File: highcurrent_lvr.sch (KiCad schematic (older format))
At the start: 8 parts, among them J1 Conn_01x02_Female, J2 Conn_01x02_Female

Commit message: fixed pcb layout
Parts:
- removed D1, D2, D3: LED, LED_SMD:LED_0805_2012Metric_Pad1.15x1.40mm_HandSolder, symbol Device:LED
- removed R7, R8, R9: 1k, Resistor_SMD:R_0805_2012Metric_Pad1.20x1.40mm_HandSolder, symbol Device:R
- renumbered J1 to POWER_IN1, J2 to POWER_OUT1
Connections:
- net GND: now also POWER_OUT1.1 (Pin_1); no longer POWER_OUT1.2 (Pin_2)
- net vout: now also POWER_OUT1.2 (Pin_2); no longer POWER_OUT1.1 (Pin_1)
- no-connect marks 0 -> 2
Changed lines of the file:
@@
 	1    0    0    -1
 $EndComp
-$Comp
-L Device:R R8
-U 1 1 602D43E7
-P 5000 5500
-F 0 "R8" H 5070 5546 50  0000 L CNN
-F 1 "1k" H 5070 5455 50  0000 L CNN
-F 2 "Resistor_SMD:R_0805_2012Metric_Pad1.20x1.40mm_HandSolder" V 4930 5500 50  0001 C CNN
-F 3 "~" H 5000 5500 50  0001 C CNN
-	1    5000 5500
-	0    -1   -1   0
-$EndComp
-$Comp
-L Device:R R9
-U 1 1 602D53F2
-P 5000 5300
-F 0 "R9" H 5070 5346 50  0000 L CNN
-F 1 "1k" H 5070 5255 50  0000 L CNN
-F 2 "Resistor_SMD:R_0805_2012Metric_Pad1.20x1.40mm_HandSolder" V 4930 5300 50  0001 C CNN
-F 3 "~" H 5000 5300 50  0001 C CNN
-	1    5000 5300
-	0    -1   -1   0
-$EndComp
-Wire Wire Line
-	4400 5300 4850 5300
-Wire Wire Line
-	4400 5700 4850 5700
-Wire Wire Line
-	4400 5500 4850 5500
 Wire Wire Line
 	800  800  800  1000
@@
 Wire Wire Line
 	1200 1000 1200 800
-Text Label 4400 5700 0    50   ~ 0
-error
-Text Label 4400 5300 0    50   ~ 0
-supp_error
-Text Label 4400 5500 0    50   ~ 0
-vout
-$Comp
-L Device:R R7
-U 1 1 604ED0D2
-P 5000 5700
-F 0 "R7" H 5070 5746 50  0000 L CNN
-F 1 "1k" H 5070 5655 50  0000 L CNN
-F 2 "Resistor_SMD:R_0805_2012Metric_Pad1.20x1.40mm_HandSolder" V 4930 5700 50  0001 C CNN
-F 3 "~" H 5000 5700 50  0001 C CNN
-	1    5000 5700
-	0    -1   -1   0
-$EndComp
 $Sheet
 S 6150 3050 950  500
@@
 F0 "Cutoff" 50
 F1 "Cutoff.sch" 50
-F2 "Vin" I L 6150 3150 50
+F2 "vin" I L 6150 3150 50
 F3 "Vout" O R 7100 3150 50
 F4 "GND" O R 7100 3250 50
@@
 Text Label 5650 3150 0    50   ~ 0
 reg_out
-$Comp
-L Device:LED D1
-U 1 1 602FA7E4
-P 5500 5300
-F 0 "D1" H 5493 5045 50  0000 C CNN
-F 1 "LED" H 5493 5136 50  0000 C CNN
-F 2 "LED_SMD:LED_0805_2012Metric_Pad1.15x1.40mm_HandSolder" H 5500 5300 50  0001 C CNN
-F 3 "~" H 5500 5300 50  0001 C CNN
-	1    5500 5300
-	-1   0    0    1
-$EndComp
-Wire Wire Line
-	5150 5300 5350 5300
-$Comp
-L Device:LED D2
-U 1 1 602FC079
-P 5500 5500
-F 0 "D2" H 5493 5245 50  0000 C CNN
-F 1 "LED" H 5493 5336 50  0000 C CNN
-F 2 "LED_SMD:LED_0805_2012Metric_Pad1.15x1.40mm_HandSolder" H 5500 5500 50  0001 C CNN
-F 3 "~" H 5500 5500 50  0001 C CNN
-	1    5500 5500
-	-1   0    0    1
-$EndComp
-Wire Wire Line
-	5150 5500 5350 5500
-$Comp
-L power:GND #PWR0115
-U 1 1 602FC629
-P 6200 6800
-F 0 "#PWR0115" H 6200 6550 50  0001 C CNN
-F 1 "GND" H 6205 6627 50  0000 C CNN
-F 2 "" H 6200 6800 50  0001 C CNN
-F 3 "" H 6200 6800 50  0001 C CNN
-	1    6200 6800
-	1    0    0    -1
-$EndComp
-$Comp
-L Device:LED D3
-U 1 1 602FC62F
-P 5500 5700
-F 0 "D3" H 5493 5445 50  0000 C CNN
-F 1 "LED" H 5493 5536 50  0000 C CNN
-F 2 "LED_SMD:LED_0805_2012Metric_Pad1.15x1.40mm_HandSolder" H 5500 5700 50  0001 C CNN
-F 3 "~" H 5500 5700 50  0001 C CNN
-	1    5500 5700
-	-1   0    0    1
-$EndComp
-Wire Wire Line
-	5150 5700 5350 5700
 Wire Wire Line
 	3750 3150 4200 3150
@@
 add reverse polarity protection
 $Comp
-L Connector:Conn_01x02_Female J1
+L Connector:Conn_01x02_Female POWER_IN1
 U 1 1 602E4815
 P 3550 3250
-F 0 "J1" H 3578 3226 50  0000 L CNN
+F 0 "POWER_IN1" H 3578 3226 50  0000 L CNN
 F 1 "Conn_01x02_Female" H 3578 3135 50  0000 L CNN
 F 2 "TerminalBlock_Phoenix:TerminalBlock_Phoenix_MKDS-1,5-2_1x02_P5.00mm_Horizontal" H 3550 3250 50  0001 C CNN
@@
 $EndComp
 $Comp
-L Connector:Conn_01x02_Female J2
+L Connector:Conn_01x02_Female POWER_OUT1
 U 1 1 602E8D12
-P 7850 3150
-F 0 "J2" H 7878 3126 50  0000 L CNN
-F 1 "Conn_01x02_Female" H 7878 3035 50  0000 L CNN
-F 2 "TerminalBlock_Phoenix:TerminalBlock_Phoenix_MKDS-1,5-2_1x02_P5.00mm_Horizontal" H 7850 3150 50  0001 C CNN
-F 3 "~" H 7850 3150 50  0001 C CNN
-	1    7850 3150
-	1    0    0    -1
+P 7850 3250
+F 0 "POWER_OUT1" H 7878 3226 50  0000 L CNN
+F 1 "Conn_01x02_Female" H 7878 3135 50  0000 L CNN
+F 2 "TerminalBlock_Phoenix:TerminalBlock_Phoenix_MKDS-1,5-2_1x02_P5.00mm_Horizontal" H 7850 3250 50  0001 C CNN
+F 3 "~" H 7850 3250 50  0001 C CNN
+	1    7850 3250
+	1    0    0    1
 $EndComp
-Wire Wire Line
-	5650 5300 6200 5300
-Wire Wire Line
-	5650 5500 6200 5500
-Connection ~ 6200 5500
-Wire Wire Line
-	6200 5500 6200 5300
-Wire Wire Line
-	5650 5700 6200 5700
-Connection ~ 6200 5700
-Wire Wire Line
-	6200 5700 6200 5500
-Wire Wire Line
-	6200 5700 6200 6800
+NoConn ~ 7250 3900
+NoConn ~ 5450 3900
 $EndSCHEMATC

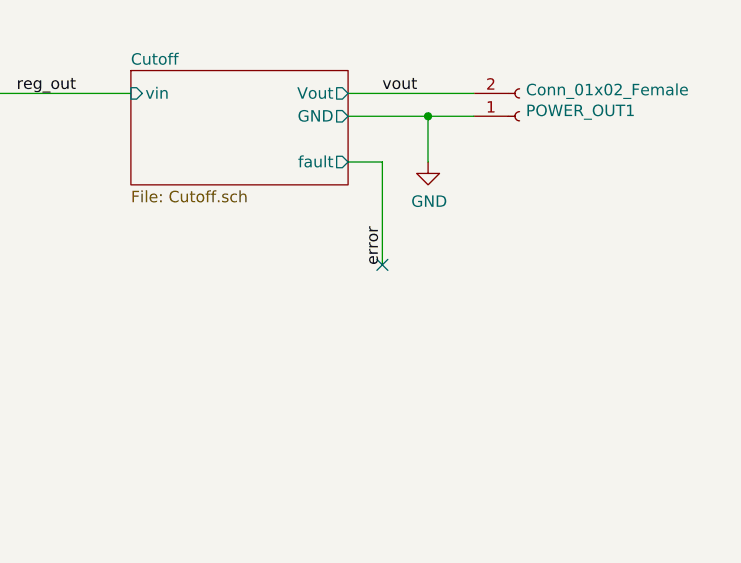
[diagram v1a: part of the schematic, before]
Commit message: added new heatsink alterantive
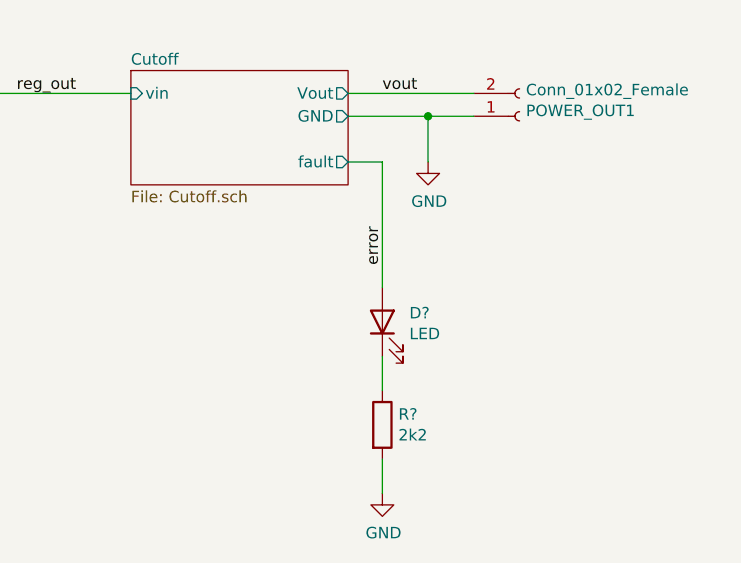
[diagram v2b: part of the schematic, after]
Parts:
- added D?: LED, symbol Device:LED
- added R?: 2k2, symbol Device:R
- POWER_IN1, POWER_OUT1: dk_pn (none) -> 277-1258-ND; ms_pn (none) -> 651-1711026
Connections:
- net GND: now also R?.2
- net error: now also D?.2 (A)
- new net: D?.1 (K), R?.1
- no-connect marks 2 -> 1
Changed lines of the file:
@@
 Wire Wire Line
 	7100 3450 7250 3450
-Wire Wire Line
-	7250 3450 7250 3900
 Text Label 5450 3900 1    50   ~ 0
 supp_error
@@
 F 2 "TerminalBlock_Phoenix:TerminalBlock_Phoenix_MKDS-1,5-2_1x02_P5.00mm_Horizontal" H 3550 3250 50  0001 C CNN
 F 3 "~" H 3550 3250 50  0001 C CNN
+F 4 "651-1711026" H 3550 3250 50  0001 C CNN "ms_pn"
+F 5 "277-1258-ND" H 3550 3250 50  0001 C CNN "dk_pn"
 	1    3550 3250
 	-1   0    0    1
@@
 F 2 "TerminalBlock_Phoenix:TerminalBlock_Phoenix_MKDS-1,5-2_1x02_P5.00mm_Horizontal" H 7850 3250 50  0001 C CNN
 F 3 "~" H 7850 3250 50  0001 C CNN
+F 4 "651-1711026" H 7850 3250 50  0001 C CNN "ms_pn"
+F 5 "277-1258-ND" H 7850 3250 50  0001 C CNN "dk_pn"
 	1    7850 3250
 	1    0    0    1
 $EndComp
-NoConn ~ 7250 3900
 NoConn ~ 5450 3900
+$Comp
+L Device:LED D?
+U 1 1 60393075
+P 7250 4150
+F 0 "D?" V 7289 4032 50  0000 R CNN
+F 1 "LED" V 7198 4032 50  0000 R CNN
+F 2 "" H 7250 4150 50  0001 C CNN
+F 3 "~" H 7250 4150 50  0001 C CNN
+	1    7250 4150
+	0    -1   -1   0
+$EndComp
+Wire Wire Line
+	7250 3450 7250 4000
+$Comp
+L Device:R R?
+U 1 1 603954F6
+P 7250 4600
+F 0 "R?" H 7320 4646 50  0000 L CNN
+F 1 "2k2" H 7320 4555 50  0000 L CNN
+F 2 "" V 7180 4600 50  0001 C CNN
+F 3 "~" H 7250 4600 50  0001 C CNN
+	1    7250 4600
+	1    0    0    -1
+$EndComp
+$Comp
+L power:GND #PWR?
+U 1 1 60395E84
+P 7250 4900
+F 0 "#PWR?" H 7250 4650 50  0001 C CNN
+F 1 "GND" H 7255 4727 50  0000 C CNN
+F 2 "" H 7250 4900 50  0001 C CNN
+F 3 "" H 7250 4900 50  0001 C CNN
+	1    7250 4900
+	1    0    0    -1
+$EndComp
+Wire Wire Line
+	7250 4900 7250 4750
+Wire Wire Line
+	7250 4450 7250 4300
 $EndSCHEMATC

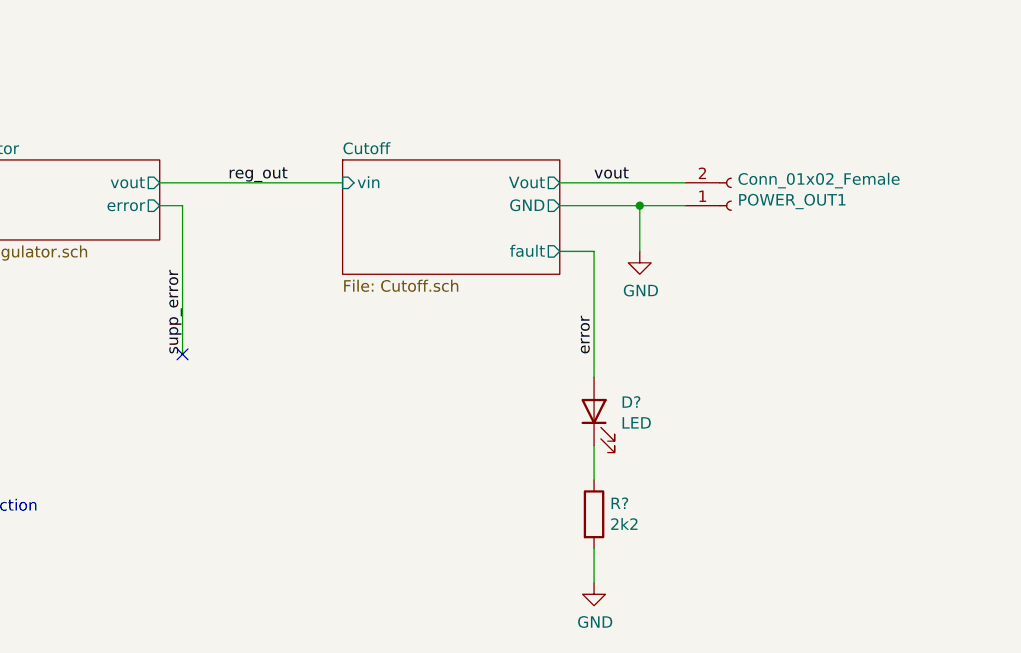
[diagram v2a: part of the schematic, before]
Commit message: changed layout for heat sink w/ issue #1
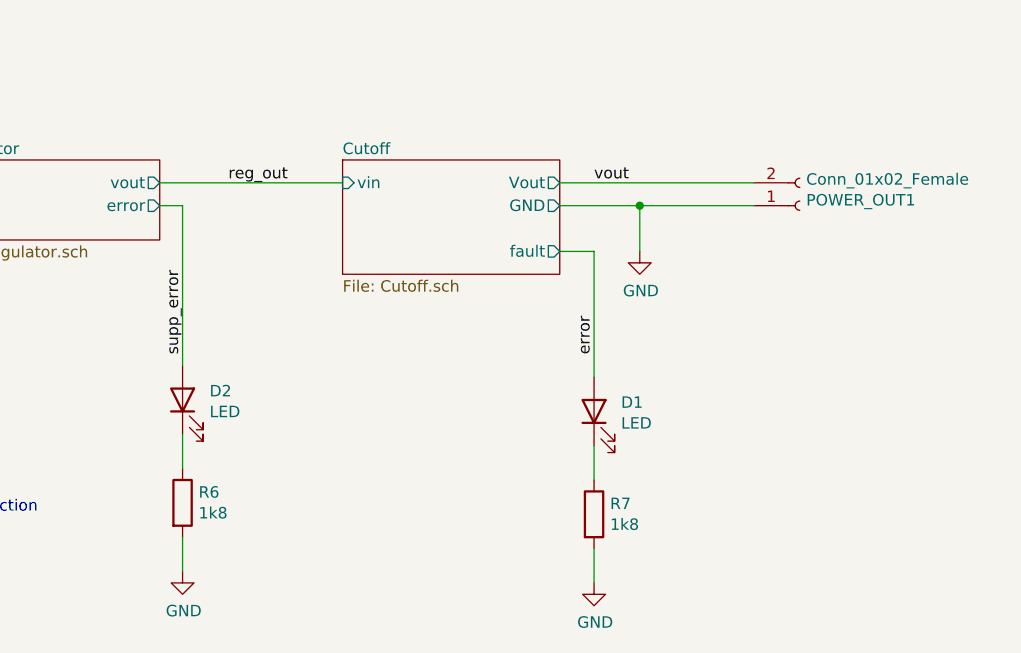
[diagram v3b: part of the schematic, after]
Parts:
- added D2: LED, LED_SMD:LED_0805_2012Metric_Pad1.15x1.40mm_HandSolder, symbol Device:LED
- added R6: 1k8, Resistor_SMD:R_0805_2012Metric_Pad1.20x1.40mm_HandSolder, symbol Device:R
- D1: renamed from D?; footprint (none) -> LED_SMD:LED_0805_2012Metric_Pad1.15x1.40mm_HandSolder; dk_pn (none) -> 754-2044-1-ND; ms_pn (none) -> 604-APTD2012LSURCK
- POWER_IN1, POWER_OUT1: footprint TerminalBlock_Phoenix:TerminalBlock_Phoenix_MKDS-1,5-2_1x02_P5.00mm_Horizontal -> wire-connector-lib:connector-wire-3cm2-2pin-smd
- R7: renamed from R?; value 2k2 -> 1k8; footprint (none) -> Resistor_SMD:R_0805_2012Metric_Pad1.20x1.40mm_HandSolder; dk_pn (none) -> 541-10510-1-ND; ms_pn (none) -> 71-RCS08051K80FKEA
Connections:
- net GND: now also R6.2
- net supp_error: now also D2.2 (A)
- new net: D2.1 (K), R6.1
- no-connect marks 1 -> 0
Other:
- moved on the sheet: POWER_OUT1
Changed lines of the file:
@@
 $EndSheet
-Wire Wire Line
-	7100 3150 7650 3150
 Wire Wire Line
 	5350 3150 6150 3150
@@
 Wire Wire Line
 	5350 3250 5450 3250
-Wire Wire Line
-	5450 3250 5450 3900
 Wire Wire Line
 	7100 3250 7450 3250
@@
 Connection ~ 7450 3250
 Wire Wire Line
-	7450 3250 7650 3250
+	7450 3250 7950 3250
 Text Notes 3750 4600 0    50   ~ 0
 add reverse polarity protection
@@
 F 0 "POWER_IN1" H 3578 3226 50  0000 L CNN
 F 1 "Conn_01x02_Female" H 3578 3135 50  0000 L CNN
-F 2 "TerminalBlock_Phoenix:TerminalBlock_Phoenix_MKDS-1,5-2_1x02_P5.00mm_Horizontal" H 3550 3250 50  0001 C CNN
+F 2 "wire-connector-lib:connector-wire-3cm2-2pin-smd" H 3550 3250 50  0001 C CNN
 F 3 "~" H 3550 3250 50  0001 C CNN
 F 4 "651-1711026" H 3550 3250 50  0001 C CNN "ms_pn"
@@
 L Connector:Conn_01x02_Female POWER_OUT1
 U 1 1 602E8D12
-P 7850 3250
-F 0 "POWER_OUT1" H 7878 3226 50  0000 L CNN
-F 1 "Conn_01x02_Female" H 7878 3135 50  0000 L CNN
-F 2 "TerminalBlock_Phoenix:TerminalBlock_Phoenix_MKDS-1,5-2_1x02_P5.00mm_Horizontal" H 7850 3250 50  0001 C CNN
-F 3 "~" H 7850 3250 50  0001 C CNN
-F 4 "651-1711026" H 7850 3250 50  0001 C CNN "ms_pn"
-F 5 "277-1258-ND" H 7850 3250 50  0001 C CNN "dk_pn"
-	1    7850 3250
+P 8150 3250
+F 0 "POWER_OUT1" H 8178 3226 50  0000 L CNN
+F 1 "Conn_01x02_Female" H 8178 3135 50  0000 L CNN
+F 2 "wire-connector-lib:connector-wire-3cm2-2pin-smd" H 8150 3250 50  0001 C CNN
+F 3 "~" H 8150 3250 50  0001 C CNN
+F 4 "651-1711026" H 8150 3250 50  0001 C CNN "ms_pn"
+F 5 "277-1258-ND" H 8150 3250 50  0001 C CNN "dk_pn"
+	1    8150 3250
 	1    0    0    1
 $EndComp
-NoConn ~ 5450 3900
 $Comp
-L Device:LED D?
+L Device:LED D1
 U 1 1 60393075
 P 7250 4150
-F 0 "D?" V 7289 4032 50  0000 R CNN
+F 0 "D1" V 7289 4032 50  0000 R CNN
 F 1 "LED" V 7198 4032 50  0000 R CNN
-F 2 "" H 7250 4150 50  0001 C CNN
+F 2 "LED_SMD:LED_0805_2012Metric_Pad1.15x1.40mm_HandSolder" H 7250 4150 50  0001 C CNN
 F 3 "~" H 7250 4150 50  0001 C CNN
+F 4 "754-2044-1-ND" H 7250 4150 50  0001 C CNN "dk_pn"
+F 5 "604-APTD2012LSURCK" H 7250 4150 50  0001 C CNN "ms_pn"
 	1    7250 4150
 	0    -1   -1   0
@@
 	7250 3450 7250 4000
 $Comp
-L Device:R R?
+L Device:R R7
 U 1 1 603954F6
 P 7250 4600
-F 0 "R?" H 7320 4646 50  0000 L CNN
-F 1 "2k2" H 7320 4555 50  0000 L CNN
-F 2 "" V 7180 4600 50  0001 C CNN
+F 0 "R7" H 7320 4646 50  0000 L CNN
+F 1 "1k8" H 7320 4555 50  0000 L CNN
+F 2 "Resistor_SMD:R_0805_2012Metric_Pad1.20x1.40mm_HandSolder" V 7180 4600 50  0001 C CNN
 F 3 "~" H 7250 4600 50  0001 C CNN
+F 4 "541-10510-1-ND" H 7250 4600 50  0001 C CNN "dk_pn"
+F 5 "71-RCS08051K80FKEA" H 7250 4600 50  0001 C CNN "ms_pn"
 	1    7250 4600
 	1    0    0    -1
 $EndComp
 $Comp
-L power:GND #PWR?
+L power:GND #PWR0108
 U 1 1 60395E84
 P 7250 4900
-F 0 "#PWR?" H 7250 4650 50  0001 C CNN
+F 0 "#PWR0108" H 7250 4650 50  0001 C CNN
 F 1 "GND" H 7255 4727 50  0000 C CNN
 F 2 "" H 7250 4900 50  0001 C CNN
@@
 Wire Wire Line
 	7250 4450 7250 4300
+$Comp
+L Device:LED D2
+U 1 1 603BAE9B
+P 5450 4100
+F 0 "D2" V 5489 3982 50  0000 R CNN
+F 1 "LED" V 5398 3982 50  0000 R CNN
+F 2 "LED_SMD:LED_0805_2012Metric_Pad1.15x1.40mm_HandSolder" H 5450 4100 50  0001 C CNN
+F 3 "~" H 5450 4100 50  0001 C CNN
+F 4 "754-2044-1-ND" H 5450 4100 50  0001 C CNN "dk_pn"
+F 5 "604-APTD2012LSURCK" H 5450 4100 50  0001 C CNN "ms_pn"
+	1    5450 4100
+	0    -1   -1   0
+$EndComp
+$Comp
+L Device:R R6
+U 1 1 603BAEA3
+P 5450 4550
+F 0 "R6" H 5520 4596 50  0000 L CNN
+F 1 "1k8" H 5520 4505 50  0000 L CNN
+F 2 "Resistor_SMD:R_0805_2012Metric_Pad1.20x1.40mm_HandSolder" V 5380 4550 50  0001 C CNN
+F 3 "~" H 5450 4550 50  0001 C CNN
+F 4 "541-10510-1-ND" H 5450 4550 50  0001 C CNN "dk_pn"
+F 5 "71-RCS08051K80FKEA" H 5450 4550 50  0001 C CNN "ms_pn"
+	1    5450 4550
+	1    0    0    -1
+$EndComp
+$Comp
+L power:GND #PWR0114
+U 1 1 603BAEA9
+P 5450 4850
+F 0 "#PWR0114" H 5450 4600 50  0001 C CNN
+F 1 "GND" H 5455 4677 50  0000 C CNN
+F 2 "" H 5450 4850 50  0001 C CNN
+F 3 "" H 5450 4850 50  0001 C CNN
+	1    5450 4850
+	1    0    0    -1
+$EndComp
+Wire Wire Line
+	5450 4850 5450 4700
+Wire Wire Line
+	5450 4400 5450 4250
+Wire Wire Line
+	5450 3250 5450 3950
+Wire Wire Line
+	7100 3150 7950 3150
 $EndSCHEMATC
